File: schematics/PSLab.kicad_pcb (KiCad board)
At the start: 4 copper layers, 99 x 53.3 mm, 182 parts, among them J1 DoublePins, J11 Li-Ion Battery, J2 Power Pins, J3 Wave Generator, J4 I2C, J5 I2C, J6 ESP01, J7 UART, J9 SPI, P1 SDCard, Q1 MMBT3906, Q2 MMBT3904, Q3 MMBT3906, Q4 Q_NMOS_DGS, SW1 BOOT, SW2 MCLR Reset, SW3 USB_C - Generic, U1 LDFM33PUR, U10 TL082, U11 TL082, U12 MCP4728, U13 MCP6S21, U14 MCP6S21, U15 CP2102N, U16 SP0503BAHT, U18 LTC4040, U19 TC1240A, U2 74HC126, U3 PIC24EP256GP204, U4 DS1307Z+, U5 TC7660, U7 LM324, U8 TL082, U9 TL082, X2 32.768 kHz, Y1 12 MHz

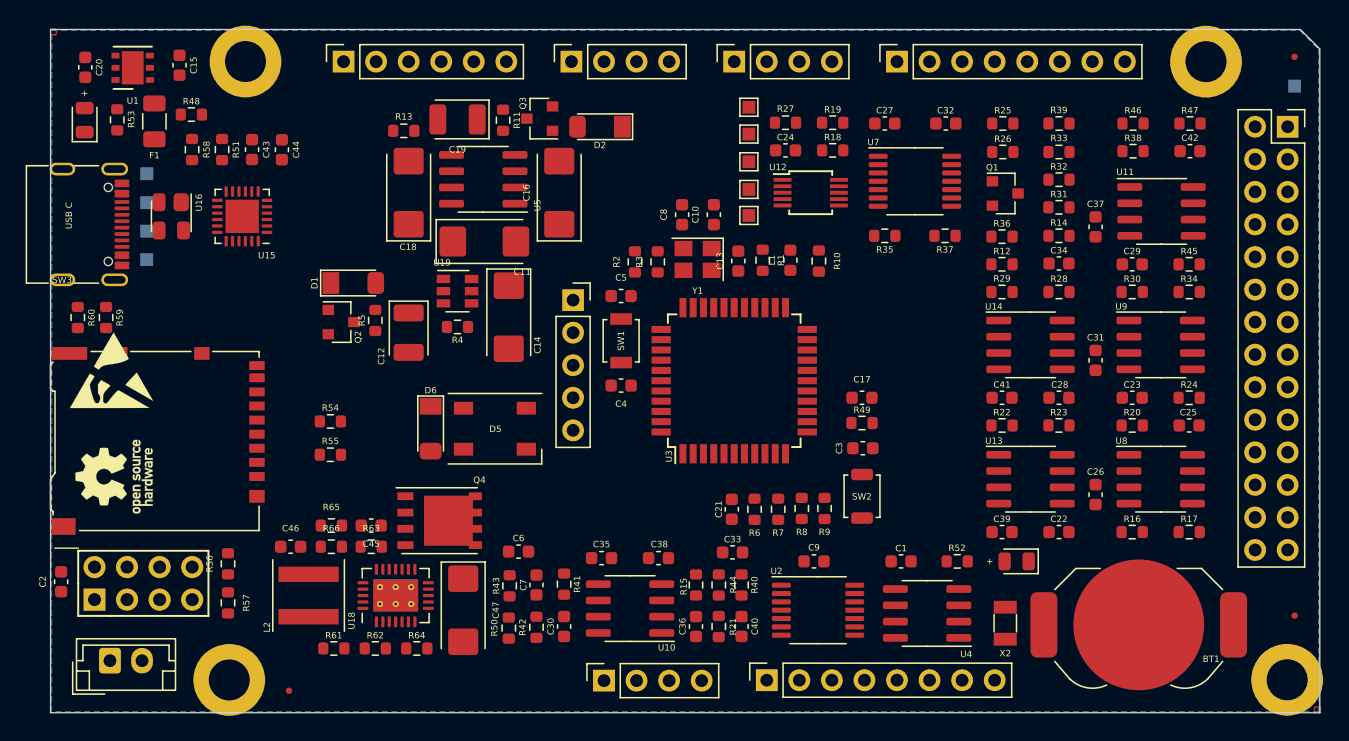
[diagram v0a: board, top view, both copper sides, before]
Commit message: refactor: basic routing without ground traces
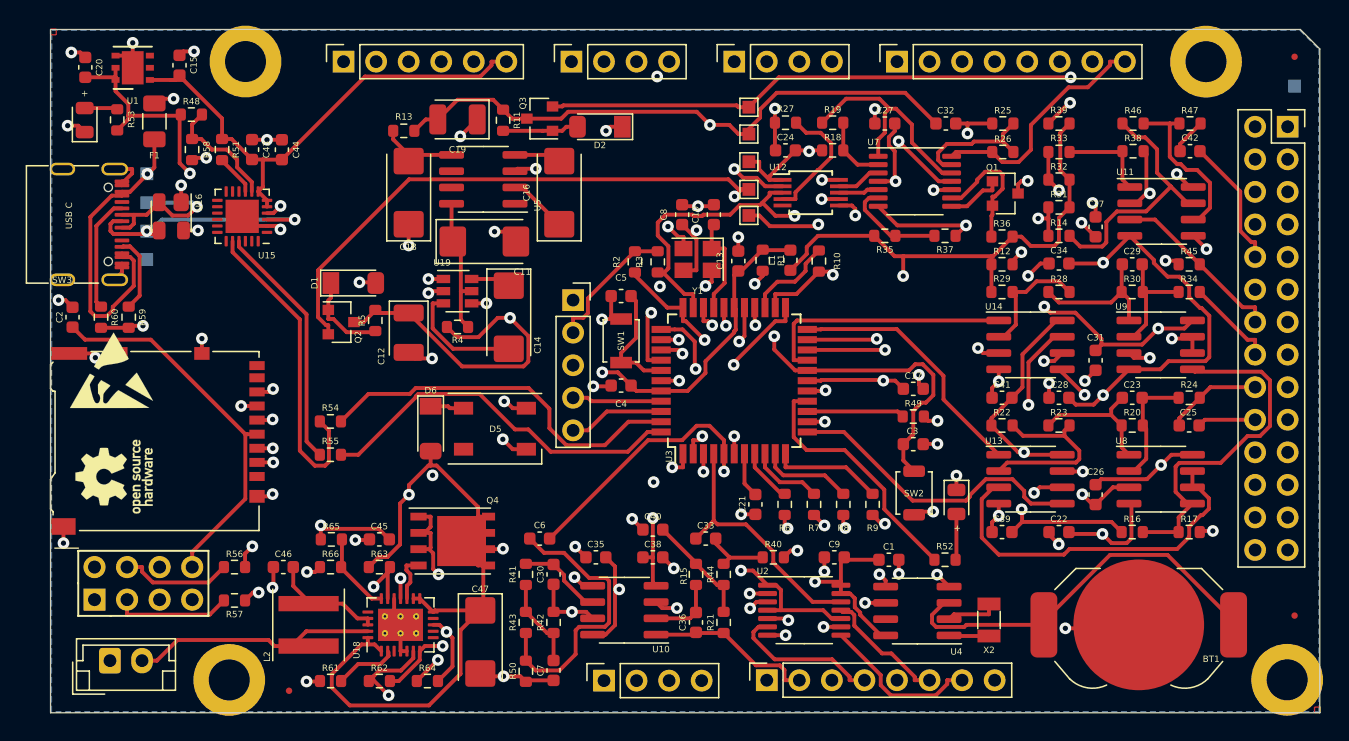
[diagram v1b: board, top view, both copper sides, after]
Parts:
- moved C2 20.7 mm to (92.7, 82.7)
- moved C40 10.2 mm to (137.9, 99.3), turned to 180 degrees
- moved C7 6.80 mm to (130.2, 110.3), turned to 270 degrees
- moved D3 6.60 mm to (161.6, 97.1), turned to 270 degrees
- moved C30 4.15 mm to (130.2, 102.8)
- moved SW2 4.07 mm to (158.3, 96.4)
- moved C17 4.06 mm to (158.2, 88.3)
- moved R49 4.03 mm to (158.2, 90.5)
- moved C3 3.95 mm to (158.2, 92.6)
- moved R9 3.76 mm to (155.1, 97.3)
- moved R50 3.62 mm to (128.0, 110.3)
- moved R40 3.28 mm to (147.3, 101.5), turned to 180 degrees
- moved R8 3.25 mm to (152.8, 97.3)
- moved R43 3.13 mm to (128.0, 106.5)
- moved R41 3.08 mm to (128.0, 102.8), turned to 90 degrees
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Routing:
- net +3V3: track 0.00 -> 225.9 mm, vias 0 -> 1
- net +5V: track 0.00 -> 182.1 mm, vias 0 -> 6
- net GND: track 0.00 -> 140.8 mm, vias 0 -> 73
- net SDO: track 0.00 -> 133.2 mm, vias 0 -> 4
- net +6V: track 0.00 -> 125.7 mm, vias 0 -> 6
- net VDDA: track 0.00 -> 124.1 mm, vias 0 -> 5
- net SCK: track 0.00 -> 123.2 mm, vias 0 -> 6
- net -6V: track 0.00 -> 107.7 mm, vias 0 -> 4
- net +10V: track 0.00 -> 107.0 mm, vias 0 -> 5
- net -10V: track 0.00 -> 106.4 mm, vias 0 -> 3
- net SDA: track 0.00 -> 84.9 mm, vias 0 -> 2
- net SCL: track 0.00 -> 81.9 mm, vias 0 -> 3
- net /VINPUT: track 0.00 -> 76.3 mm, vias 0 -> 5
- net SDI: track 0.00 -> 75.4 mm, vias 0 -> 3
- net RxD2: track 0.00 -> 55.8 mm
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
